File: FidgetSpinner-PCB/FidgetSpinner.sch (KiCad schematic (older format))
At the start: 38 parts, among them J1 Holes, Q1 Q_Photo_NPN, SW1 SW_SPST, SW2 button, U1 ATmega328P-AU, Y1 16M

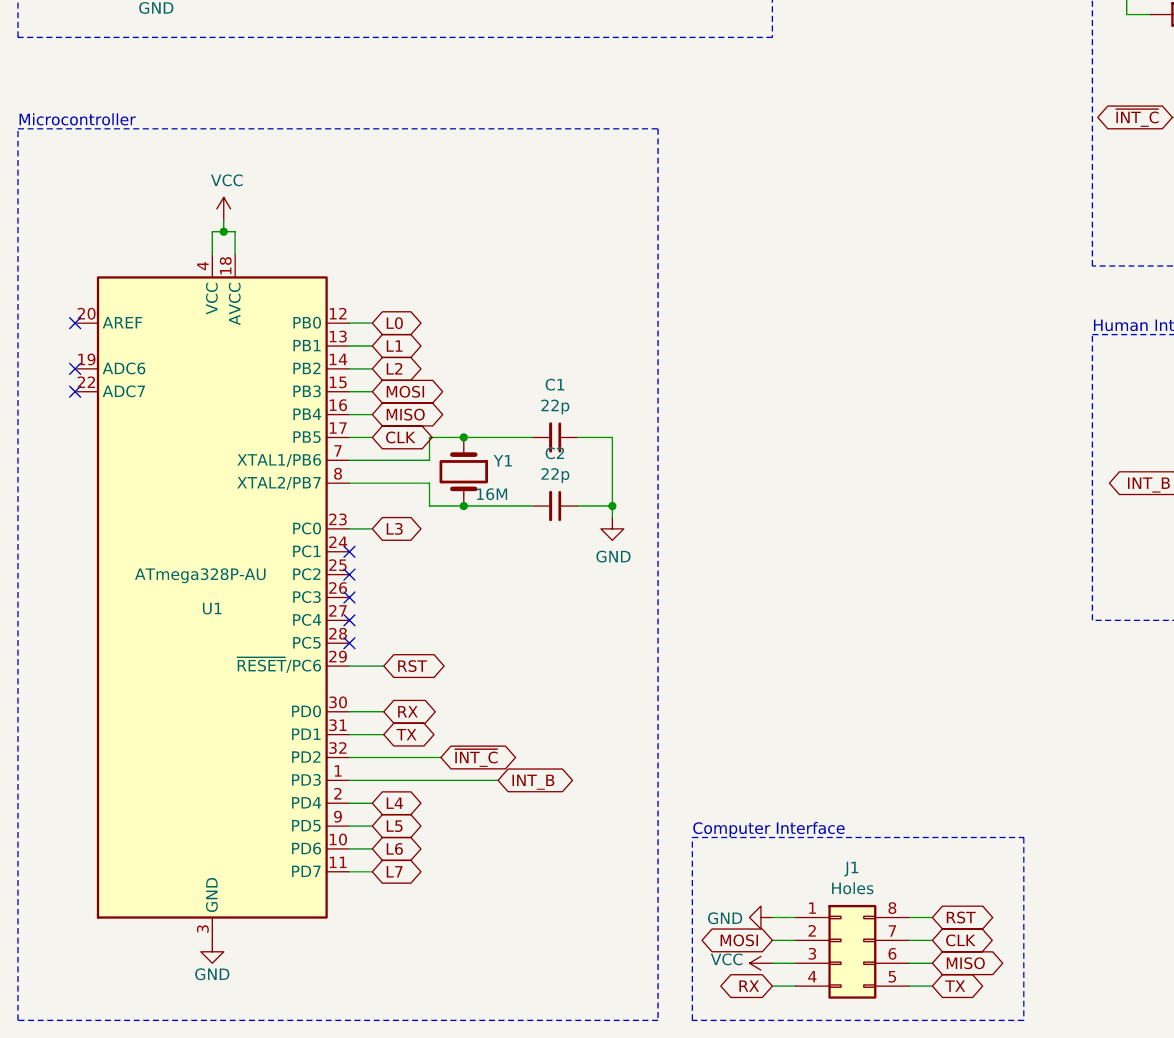
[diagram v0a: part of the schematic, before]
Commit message: changed to STM32L0 MCU
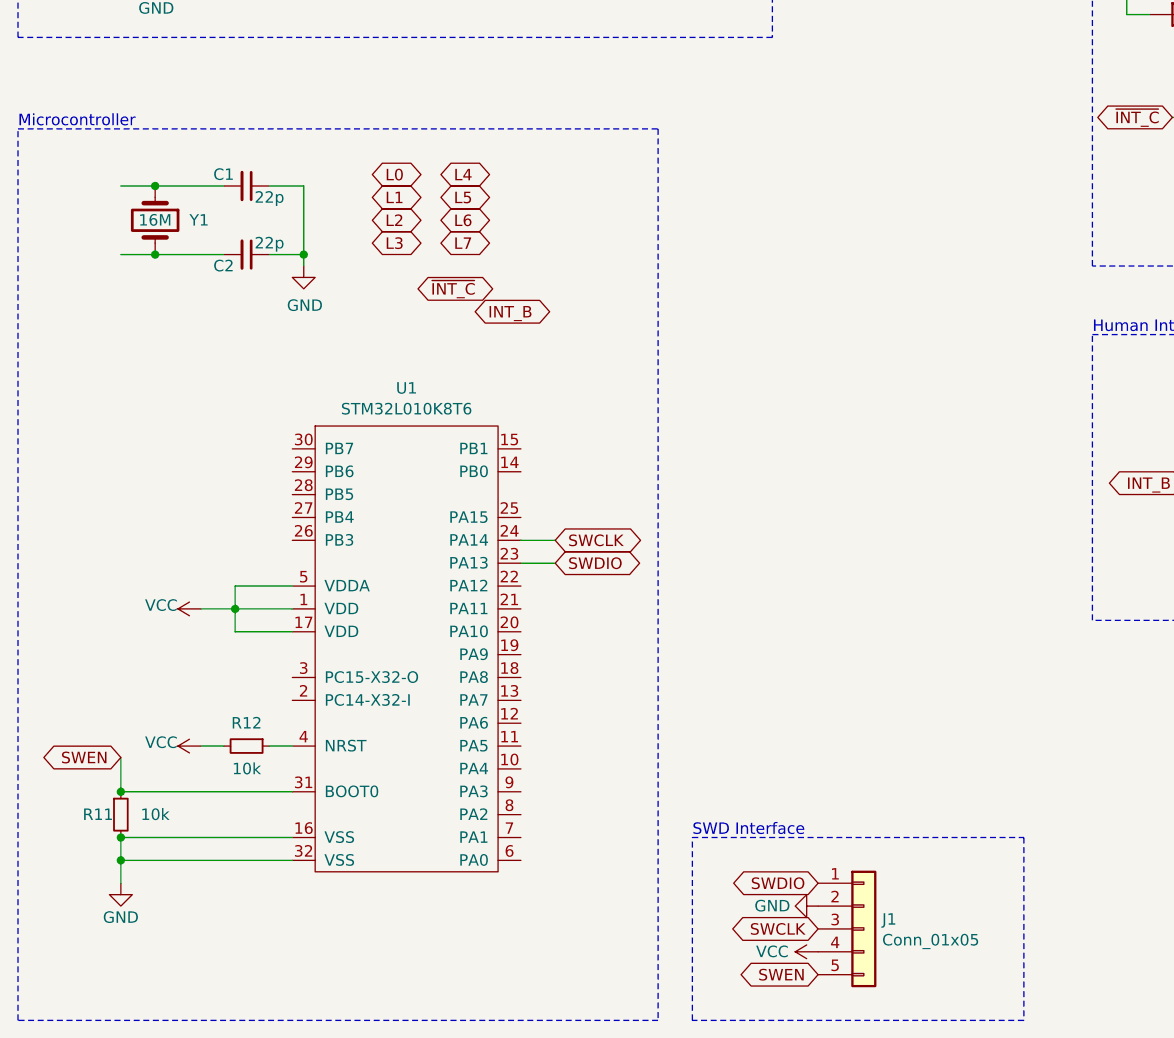
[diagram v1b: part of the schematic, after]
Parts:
- removed J1: Holes, Connector_PinHeader_2.54mm:PinHeader_2x04_P2.54mm_Vertical, symbol Connector_Generic:Conn_02x04_Counter_Clockwise
- removed U1: ATmega328P-AU, Package_QFP:TQFP-32_7x7mm_P0.8mm, symbol MCU_Microchip_ATmega:ATmega328P-AU
- added J1: Conn_01x05, symbol Connector_Generic:Conn_01x05
- added R11, R12: 10k, Resistor_SMD:R_0805_2012Metric_Pad1.20x1.40mm_HandSolder, symbol Device:R_Small
- added U1: STM32L010K8T6, symbol WYW_Library:STM32L010K8T6
- BT1, BT2, BT3: footprint Battery:BatteryHolder_ComfortableElectronic_CH273-2450_1x2450 -> Battery:BatteryHolder_Keystone_1060_1x2032
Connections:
- net GND: now also J1.2 (Pin_2), R11.2, U1.16 (VSS), U1.32 (VSS)
- net VCC: now also J1.4 (Pin_4), R12.2, U1.1 (VDD), U1.17 (VDD), U1.5 (VDDA)
- new net: R12.1, U1.4 (NRST)
- new net SWCLK: J1.3 (Pin_3), U1.24 (PA14)
- new net SWDIO: J1.1 (Pin_1), U1.23 (PA13)
- new net SWEN: J1.5 (Pin_5), R11.1, U1.31 (BOOT0)
- no-connect marks 8 -> 0
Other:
- note added: "SWD Interface"
- note removed: "Computer Interface"
- moved on the sheet: C1, C2, Y1

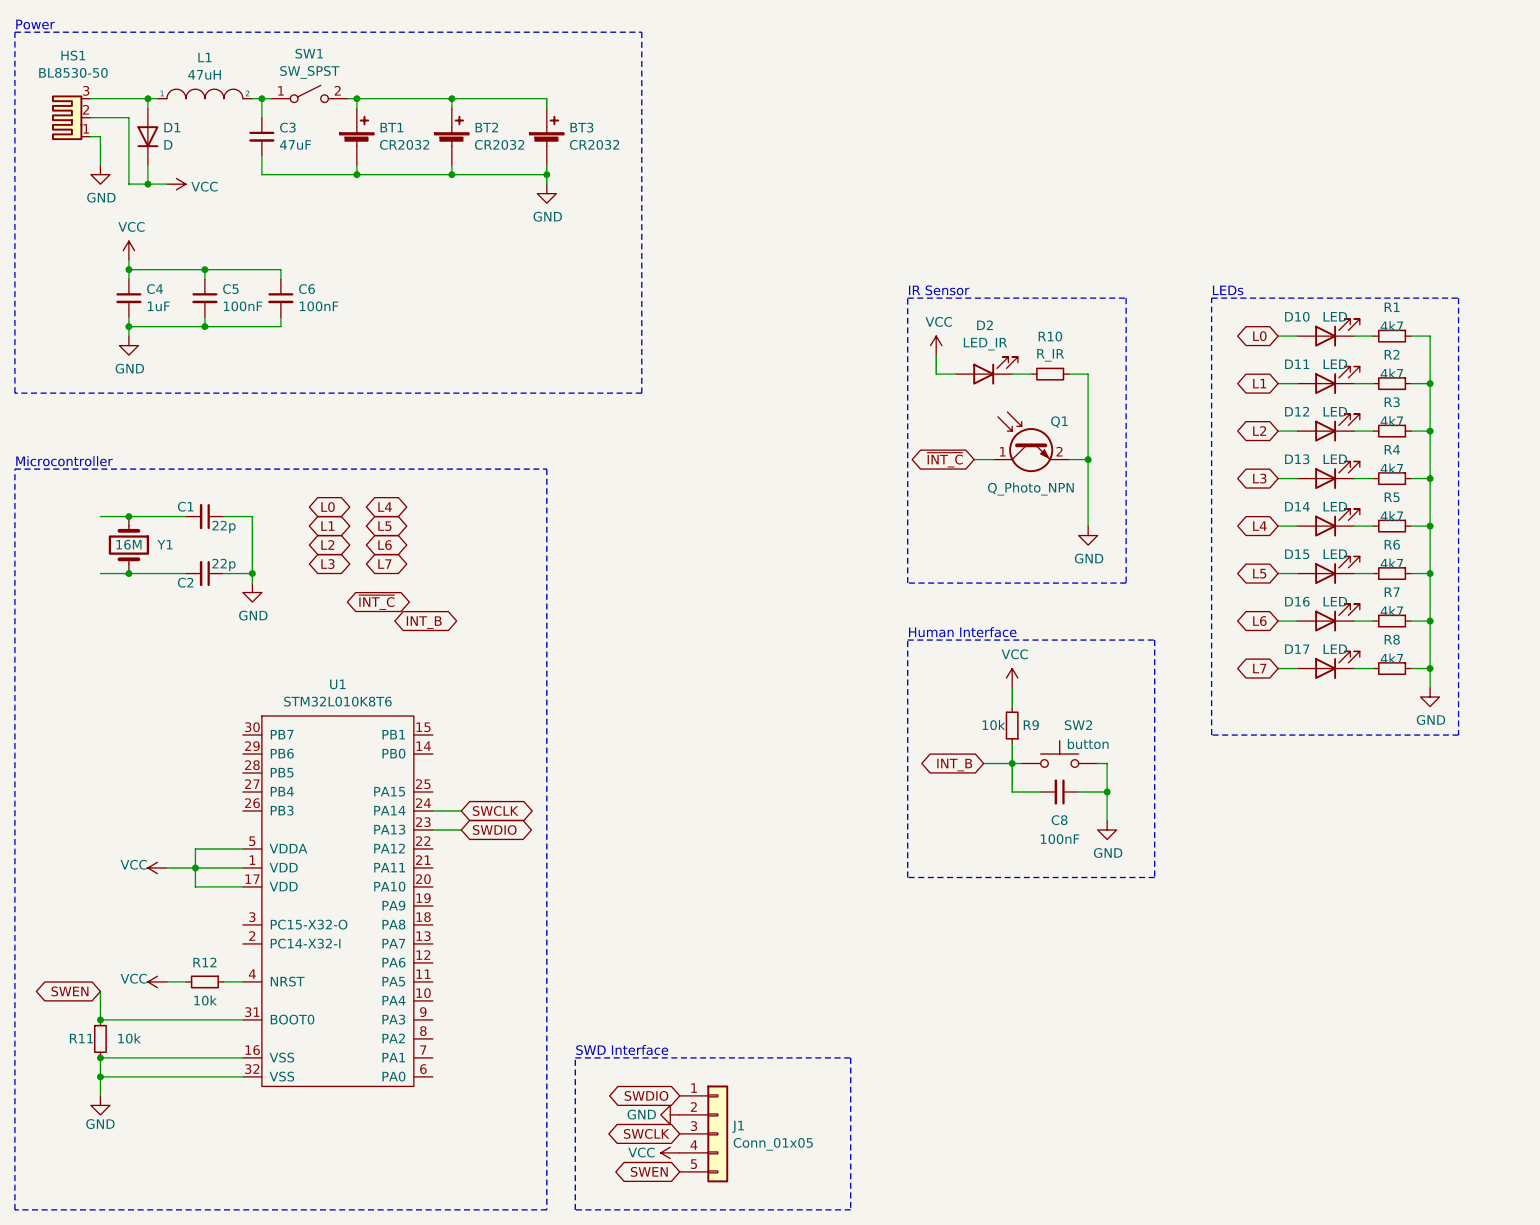
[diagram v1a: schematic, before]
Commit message: changed to STM32 and CR2450
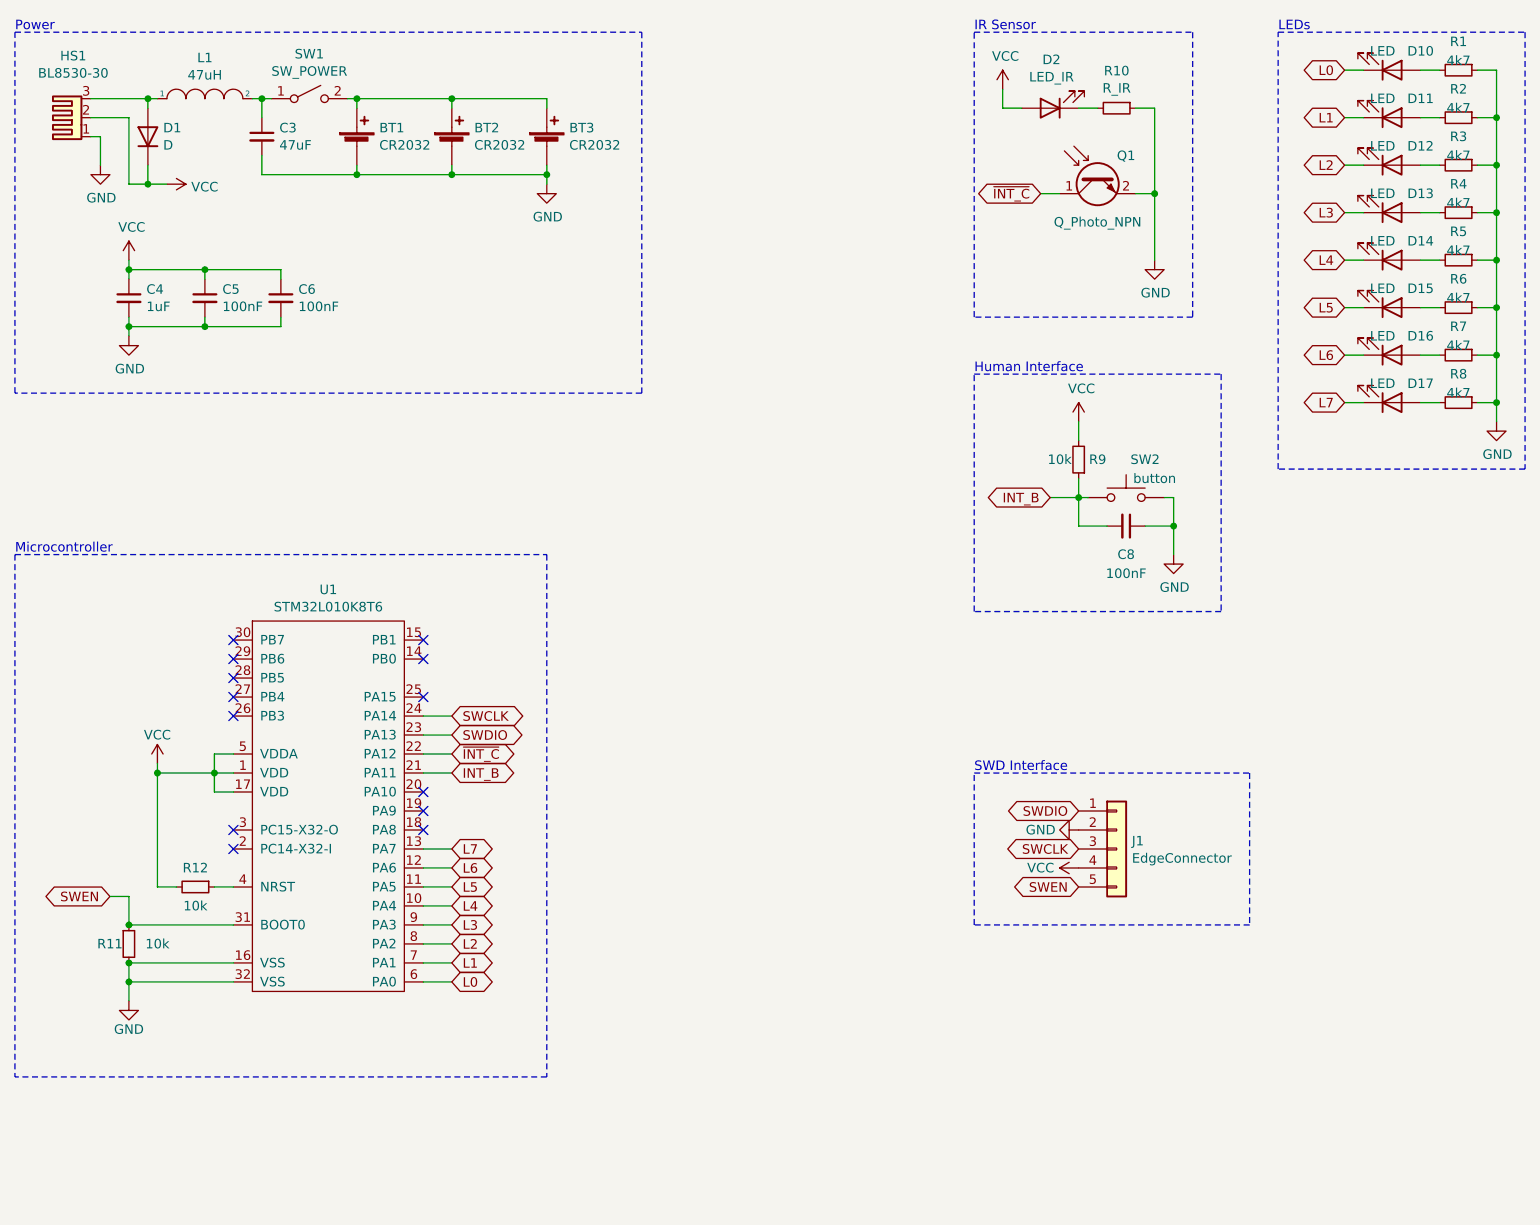
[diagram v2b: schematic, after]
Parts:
- removed C1, C2: 22p, Capacitor_SMD:C_0805_2012Metric_Pad1.18x1.45mm_HandSolder, symbol Device:C_Small
- removed Y1: 16M, Crystal:Crystal_SMD_5032-2Pin_5.0x3.2mm_HandSoldering, symbol Device:Crystal
- BT1, BT2, BT3: footprint Battery:BatteryHolder_Keystone_1060_1x2032 -> WYW_Package:CR2450_Centered
- HS1: value BL8530-50 -> BL8530-30
- J1: value Conn_01x05 -> EdgeConnector; footprint (none) -> WYW_Package:Edge_2x05_2.54
- SW1: value SW_SPST -> SW_POWER
- U1: footprint (none) -> Package_QFP:LQFP-32_7x7mm_P0.8mm
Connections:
- net INT_B: now also U1.21 (PA11)
- net L0: now also D10.1 (K), U1.6 (PA0); no longer D10.2 (A)
- net L1: now also D11.1 (K), U1.7 (PA1); no longer D11.2 (A)
- net L2: now also D12.1 (K), U1.8 (PA2); no longer D12.2 (A)
- net L3: now also D13.1 (K), U1.9 (PA3); no longer D13.2 (A)
- net L4: now also D14.1 (K), U1.10 (PA4); no longer D14.2 (A)
- net L5: now also D15.1 (K), U1.11 (PA5); no longer D15.2 (A)
- net L6: now also D16.1 (K), U1.12 (PA6); no longer D16.2 (A)
- net L7: now also D17.1 (K), U1.13 (PA7); no longer D17.2 (A)
- net ~INT_C: now also U1.22 (PA12)
- net at R1.2: now also D10.2 (A); no longer D10.1 (K)
- net at R2.2: now also D11.2 (A); no longer D11.1 (K)
- net at R3.2: now also D12.2 (A); no longer D12.1 (K)
- net at R4.2: now also D13.2 (A); no longer D13.1 (K)
- net at R5.2: now also D14.2 (A); no longer D14.1 (K)
- net at R6.2: now also D15.2 (A); no longer D15.1 (K)
- net at R7.2: now also D16.2 (A); no longer D16.1 (K)
- net at R8.2: now also D17.2 (A); no longer D17.1 (K)
- no-connect marks 0 -> 13
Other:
- moved on the sheet: C8, D10, D11, D12, D13, D14, D15, D16, D17, D2, J1, Q1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
